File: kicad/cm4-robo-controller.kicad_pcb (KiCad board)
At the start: 4 copper layers, 150 x 90 mm, 256 parts, among them CN1 SMA-KWE_C7498154, J1 KF7620-7.62-2P, J10 KF2EDGR-2.54-2P, J11 KF7620-7.62-2P, J12 KF2EDGR-2.54-2P, J13 KF2EDGR-2.54-2P, J14 KF7620-7.62-2P, J15 PM254-2-12-Z-8.5, J16 PM254-2-09-Z-8.5, J2 HX PZ2.54-2X5P TP, J3 Header-Male-2.54_2x3, J4 2541WV-2X12P, J5 Header-Male-2.54_1x3, J6 Header-Male-2.54_2x3, J7 SMA-KWE_C7498154, J8 KF2EDGR-2.54-4P, J9 KF2EDGR-2.54-3P, Q1 SP40P04NK, Q2 DMP6023LE-13, Q3 NCE6008AS, Q4 BSS138, SW1 SS-12F49-G050, U1 74LVC1G07SE-7, U10 74LVC1G07SE-7, U11 MX26631DL, U12 MAX-M10S-00B, U13 74LVC1G17SE-7, U14 74LVC1G17SE-7, U15 AP64501SP-13, U16 74LVC1G17SE-7, U17 74LVC1G07SE-7, U18 TPS70933DBVR, U19 74LVC1G17SE-7, U2 FSUSB42MUX, U3 USB2514B-I/M2, U4 AP22653W6-7, U5 TPD4EUSB30DQAR, U6 TPD4EUSB30DQAR, U7 TPD4EUSB30DQAR, U8 TPD4EUSB30DQAR, U9 TPD4EUSB30DQAR, X1 24MHz

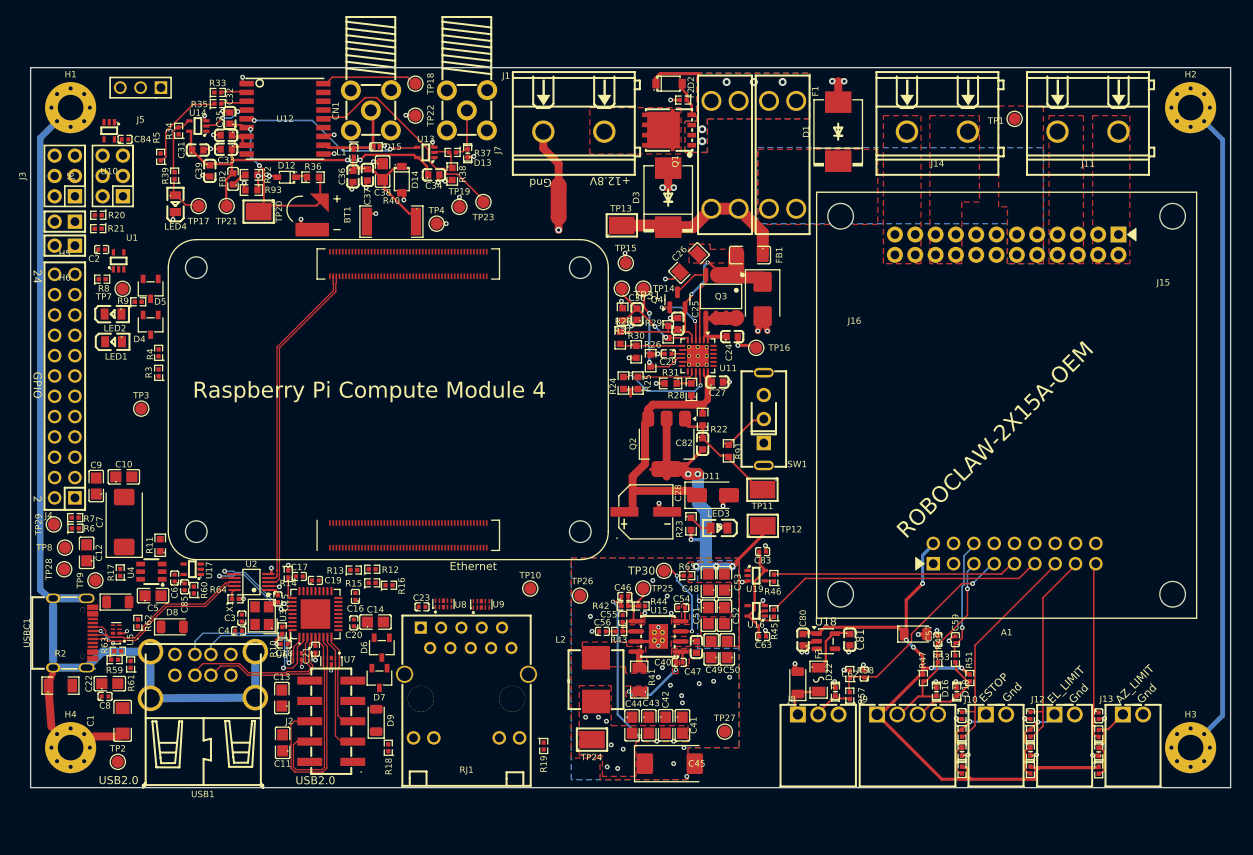
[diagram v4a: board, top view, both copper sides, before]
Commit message: PCB: swap GPS and USB areas, drop J2 and hub ports 3/4, remap J4
- Remove expansion header J2 with C22, U7, D9 and D7; disable USB2514B
  ports 3 and 4 with 10k pull-ups (R94-R97) on their D-/D+ straps.
- Remap J4 GPIO pins so they route to the CM4 connector without
  crossovers (schematic labels, notes and PCB pad nets).
- Add decoupling caps C84 (U10) and C85 (U17); add HUB_CTRL net class.
- Move USB (USB1, USBC1, hub) to the top edge and GPS (U12, CN1, J7) to
  the bottom-left; R4/R5 move with the GPS group. First-pass placement,
  all USB and GPS copper removed for manual routing.
- Relabel bottom-edge silk text for the SMA connectors.
- README and usb-power sim note updated for the two-port hub.
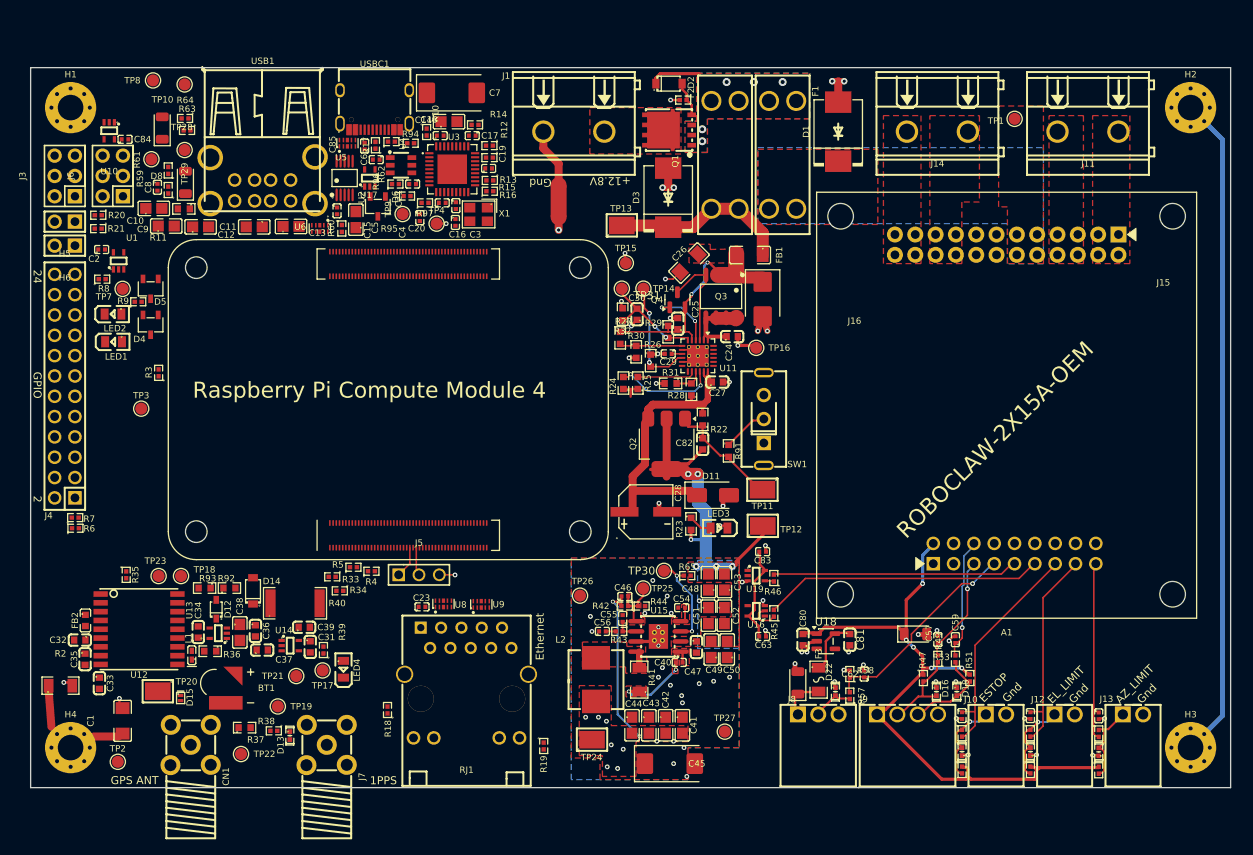
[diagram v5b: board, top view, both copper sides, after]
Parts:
- removed C22: 10uF, MyPartsIPC:CAPC2012X145N
- removed D7: BAT54C, MyPartsIPC:SOT95P280X110-3N
- removed D9: SMF6.0A, MyPartsIPC:SODFL3718X110N
- removed J2: HX PZ2.54-2X5P TP, MyParts:HDR-SMD_10P-P2.54-V-M-R2-C5-LS7.5
- removed U7: TPD4EUSB30DQAR, MyPartsIPC:SON50P100X250X60-10N
- added R94: 10kΩ, MyPartsIPC:RESC1005X40N, F.Cu at (107.5, 59.0)
- added R95: 10kΩ, MyPartsIPC:RESC1005X40N, F.Cu at (107.0, 65.7)
- added R96: 10kΩ, MyPartsIPC:RESC1005X40N, F.Cu at (105.6, 64.2)
- added R97: 10kΩ, MyPartsIPC:RESC1005X40N, F.Cu at (109.3, 66.5)
- moved TP22 82.7 mm to (86.3, 135.4), turned to 270 degrees
- moved CN1 82.5 mm to (80.0, 134.3), turned to 90 degrees
- moved J7 81.3 mm to (97.0, 134.3), turned to 90 degrees
- moved TP10 76.4 mm to (79.2, 51.7), turned to 270 degrees
- moved D13 76.1 mm to (92.4, 133.1), turned to 270 degrees
- moved R37 75.7 mm to (90.4, 132.5)
- moved USBC1 75.5 mm to (103.0, 54.9), turned to 180 degrees
- moved R38 73.9 mm to (86.8, 132.1), turned to 0 degrees
- moved D15 73.1 mm to (78.8, 128.4), turned to 270 degrees
- moved J5 70.1 mm to (108.5, 113.0), turned to 0 degrees
- moved C33 68.6 mm to (68.6, 126.5), turned to 270 degrees
- moved TP18 68.2 mm to (78.8, 113.2)
- moved R62 68.0 mm to (105.1, 58.9), turned to 0 degrees
- moved C32 67.9 mm to (66.2, 121.2), turned to 180 degrees
- moved C35 67.8 mm to (66.8, 123.5), turned to 270 degrees
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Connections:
- J4 pad 10: /CM4/SPI0_MISO -> /CM4/GPIO1
- J4 pad 11: /CM4/GPIO18 -> /CM4/GPIO19
- J4 pad 12: /CM4/SPI0_CE0 -> /CM4/SPI0_CE1
- J4 pad 13: /CM4/GPIO19 -> /CM4/GPIO0
- J4 pad 14: /CM4/SPI0_CE1 -> /CM4/SPI0_CE0
- J4 pad 15: /CM4/GPIO20 -> /CM4/SPI0_SCLK
- J4 pad 16: /CM4/I2C1_SDA -> /CM4/GPIO23
- J4 pad 17: /CM4/GPIO21 -> /CM4/SPI0_MISO
- J4 pad 18: /CM4/I2C1_SCL -> /CM4/GPIO18
- J4 pad 19: /CM4/GPIO23 -> /CM4/SPI0_MOSI
- J4 pad 20: /CM4/GPIO26 -> /CM4/GPIO17
- J4 pad 21: /CM4/GPIO27 -> /CM4/GPIO22
- J4 pad 22: /CM4/GPIO0 -> /CM4/I2C1_SCL
- J4 pad 23: /CM4/GPIO1 -> /CM4/GPIO27
- J4 pad 24: /CM4/GPIO22 -> /CM4/I2C1_SDA
- J4 pad 5: /5V -> /3V3_CM4
- J4 pad 6: /CM4/SPI0_SCLK -> /CM4/GPIO21
- J4 pad 7: /3V3_CM4 -> /5V
- J4 pad 8: /CM4/SPI0_MOSI -> /CM4/GPIO20
- J4 pad 9: /CM4/GPIO17 -> /CM4/GPIO26
- U3 pad 18: /CM4/usb/PWR3 -> unconnected-(U3-PRTPWR3/BC_EN3-Pad18)
- U3 pad 20: /CM4/usb/PWR4 -> unconnected-(U3-PRTPWR4/BC_EN4-Pad20)
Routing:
- net CHASSIS: track 195.9 -> 85.4 mm
- net /GPS/VCC: track 42.4 -> 0.00 mm, vias 2 -> 0
- net /CM4/USB2_P: track 42.3 -> 0.00 mm
- net /CM4/USB2_N: track 41.6 -> 0.00 mm
- net /CM4/usb/HD3_P: track 29.5 -> 0.00 mm
- net /GPS/VCC_RF: track 26.7 -> 0.00 mm
- net /CM4/usb/HD3_N: track 25.7 -> 0.00 mm
- net /CM4/usb/HSD2+: track 24.2 -> 0.00 mm, vias 2 -> 0
- net /CM4/usb/HSD2-: track 23.4 -> 0.00 mm
- net /GPS/EXT_1PPS: track 22.4 -> 0.00 mm, vias 2 -> 0
- net GND: track 52.9 -> 30.8 mm, vias 71 -> 44
- net /GPS/V_BCKP: track 21.3 -> 0.00 mm, vias 2 -> 0
- net /CM4/usb/HD1_N: track 21.0 -> 0.00 mm, vias 1 -> 0
- net /CM4/usb/HD2_N: track 20.3 -> 0.00 mm
- net /CM4/usb/HD1_P: track 20.3 -> 0.00 mm, vias 1 -> 0
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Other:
- board text added: "1PPS"
- board text added: "GPS ANT"
- board text removed: "USB2.0"
